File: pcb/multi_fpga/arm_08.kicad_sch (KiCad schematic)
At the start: 16 parts, among them U65 IM72D128V01XTMA1, U66 IM72D128V01XTMA1, U67 IM72D128V01XTMA1, U68 IM72D128V01XTMA1, U69 IM72D128V01XTMA1, U70 IM72D128V01XTMA1, U71 IM72D128V01XTMA1, U72 IM72D128V01XTMA1

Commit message: Fixed library and power issues.
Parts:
- C65, C66, C67, C68, C69, C70, C71, C72: symbol C -> multi_fpga:C
- U65, U66, U67, U68, U69, U70, U71, U72: symbol IM72D128 -> multi_fpga:IM72D128

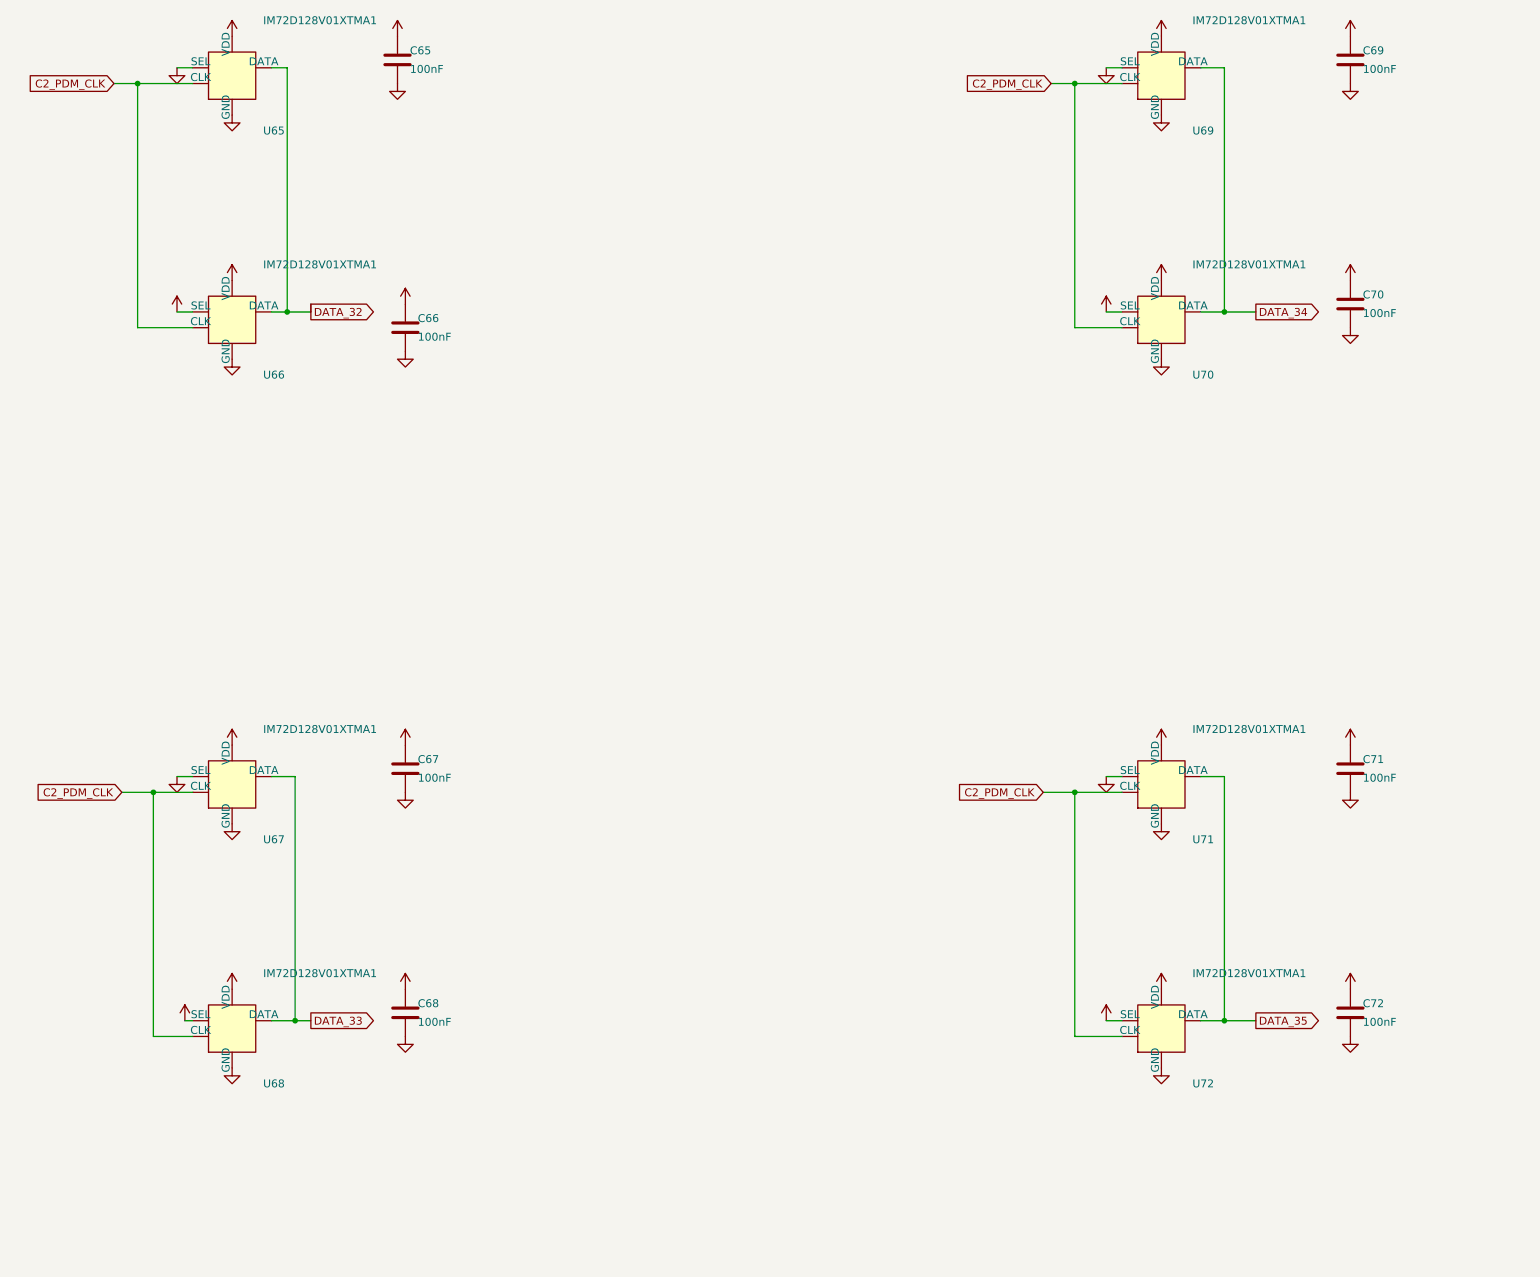
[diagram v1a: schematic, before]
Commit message: Fixed power and C ref des collisions.
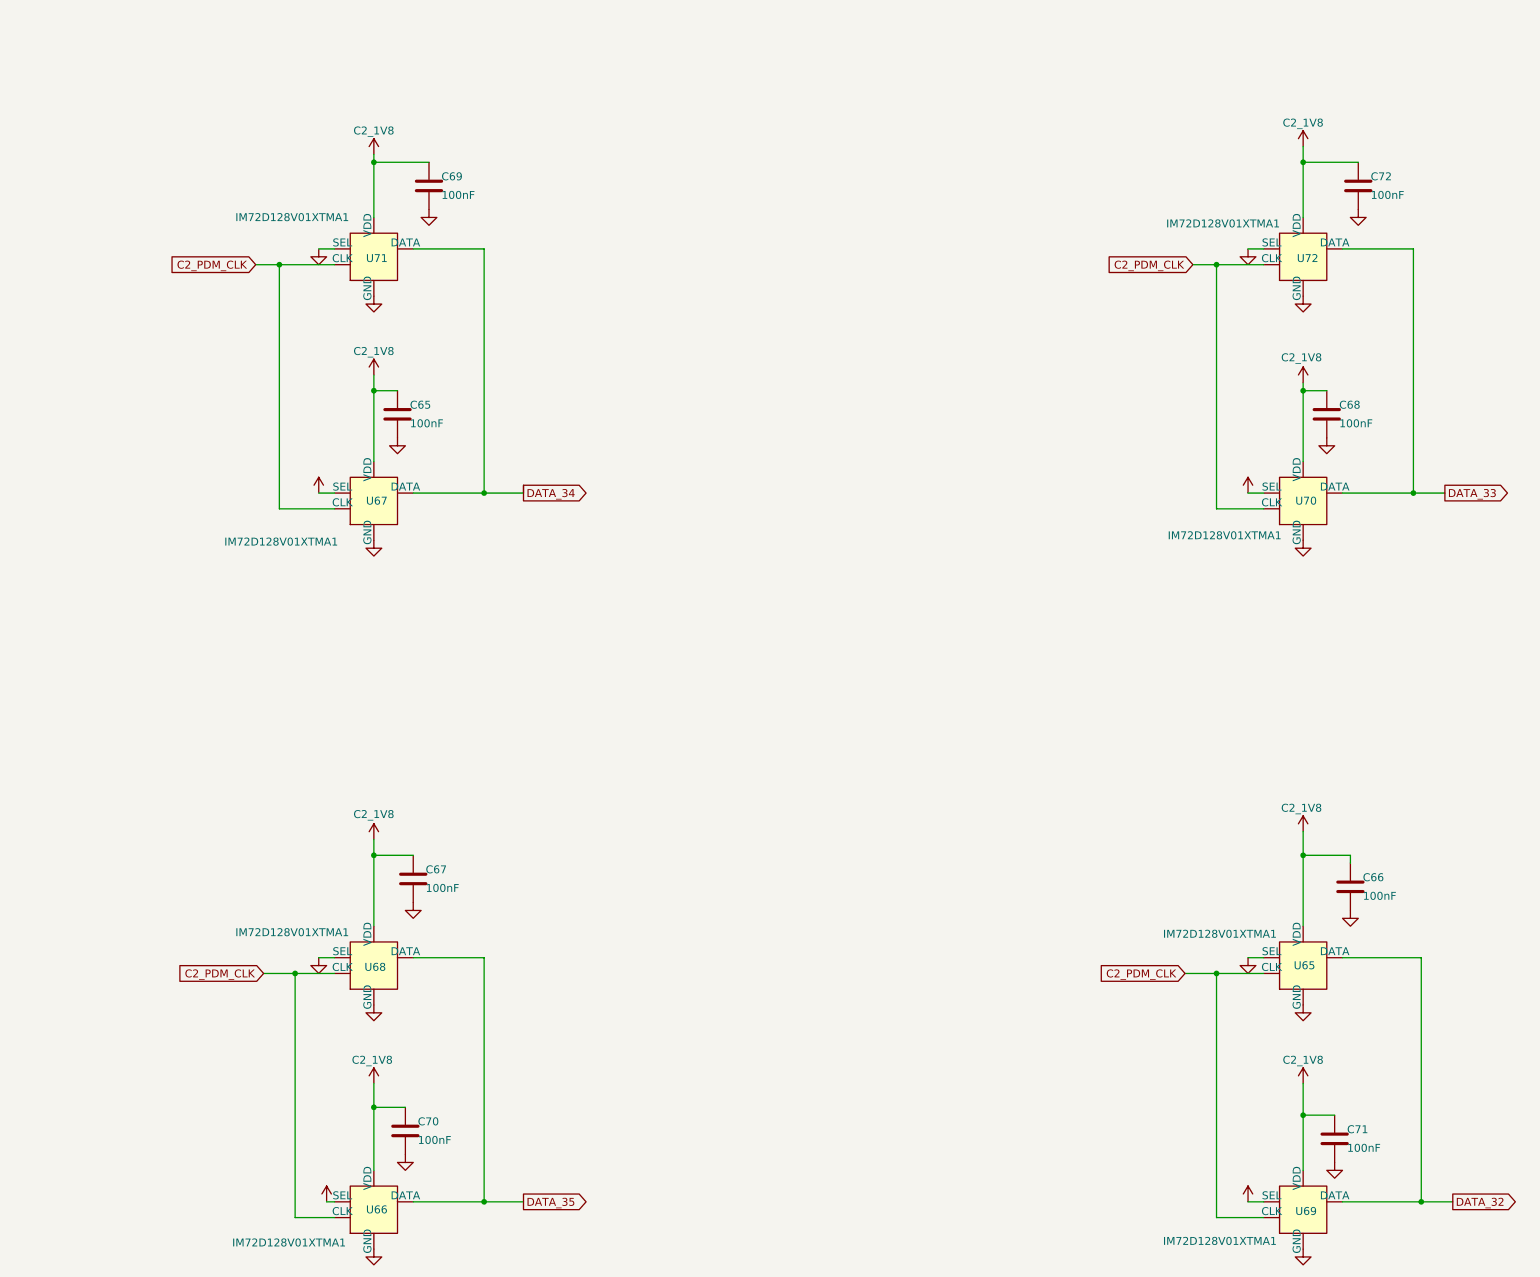
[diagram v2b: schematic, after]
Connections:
- net C2_1V8: now also U67.4 (SEL), U69.4 (SEL); no longer U68.4 (SEL), U72.4 (SEL)
- net DATA_32: now also U69.1 (DATA); no longer U66.1 (DATA)
- net DATA_33: now also U70.1 (DATA), U72.1 (DATA); no longer U67.1 (DATA), U68.1 (DATA)
- net DATA_34: now also U67.1 (DATA), U71.1 (DATA); no longer U69.1 (DATA), U70.1 (DATA)
- net DATA_35: now also U66.1 (DATA), U68.1 (DATA); no longer U71.1 (DATA), U72.1 (DATA)
- net GND: now also U68.4 (SEL), U72.4 (SEL); no longer U67.4 (SEL), U69.4 (SEL)

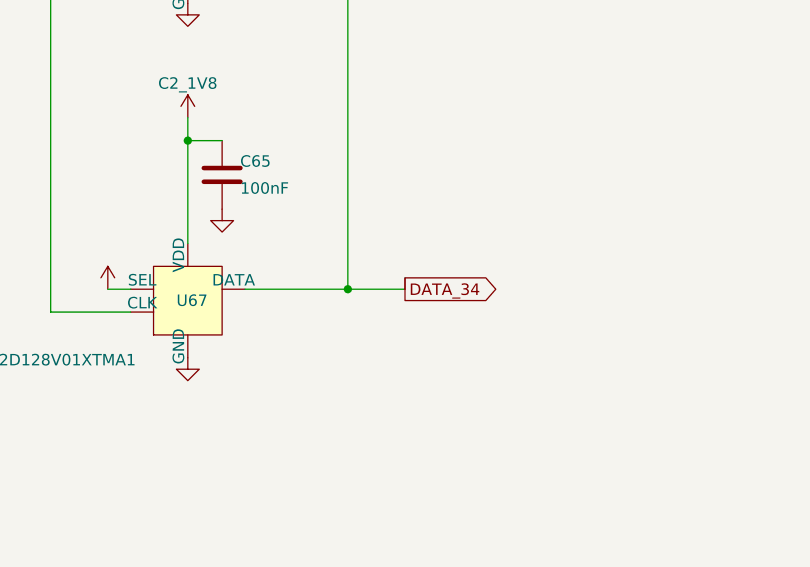
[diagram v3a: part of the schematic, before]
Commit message: Fixed regulator connection errors and dangling wire.
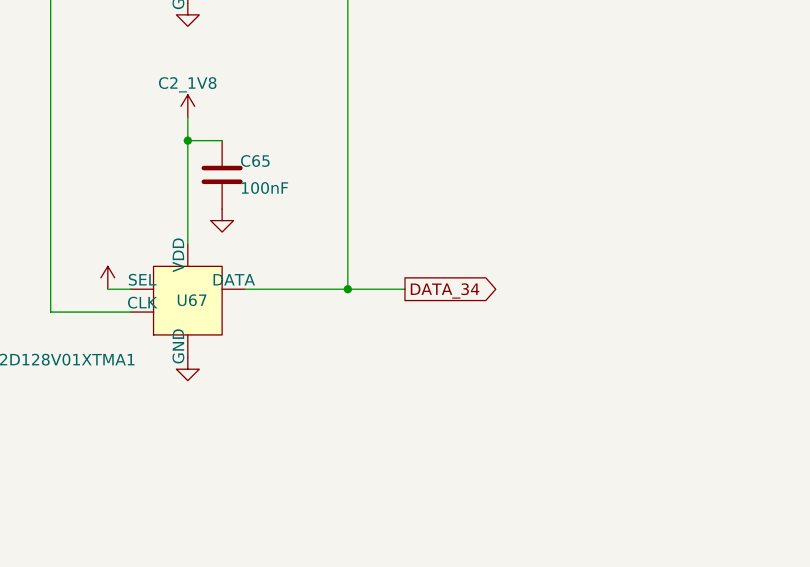
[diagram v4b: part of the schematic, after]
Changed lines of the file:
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@@
-	(wire
-		(pts
-			(xy 127 106.68) (xy 127 107.95)
-		)
-		(stroke
-			(width 0)
-			(type default)
-		)
-	)
 	(wire
 		(pts

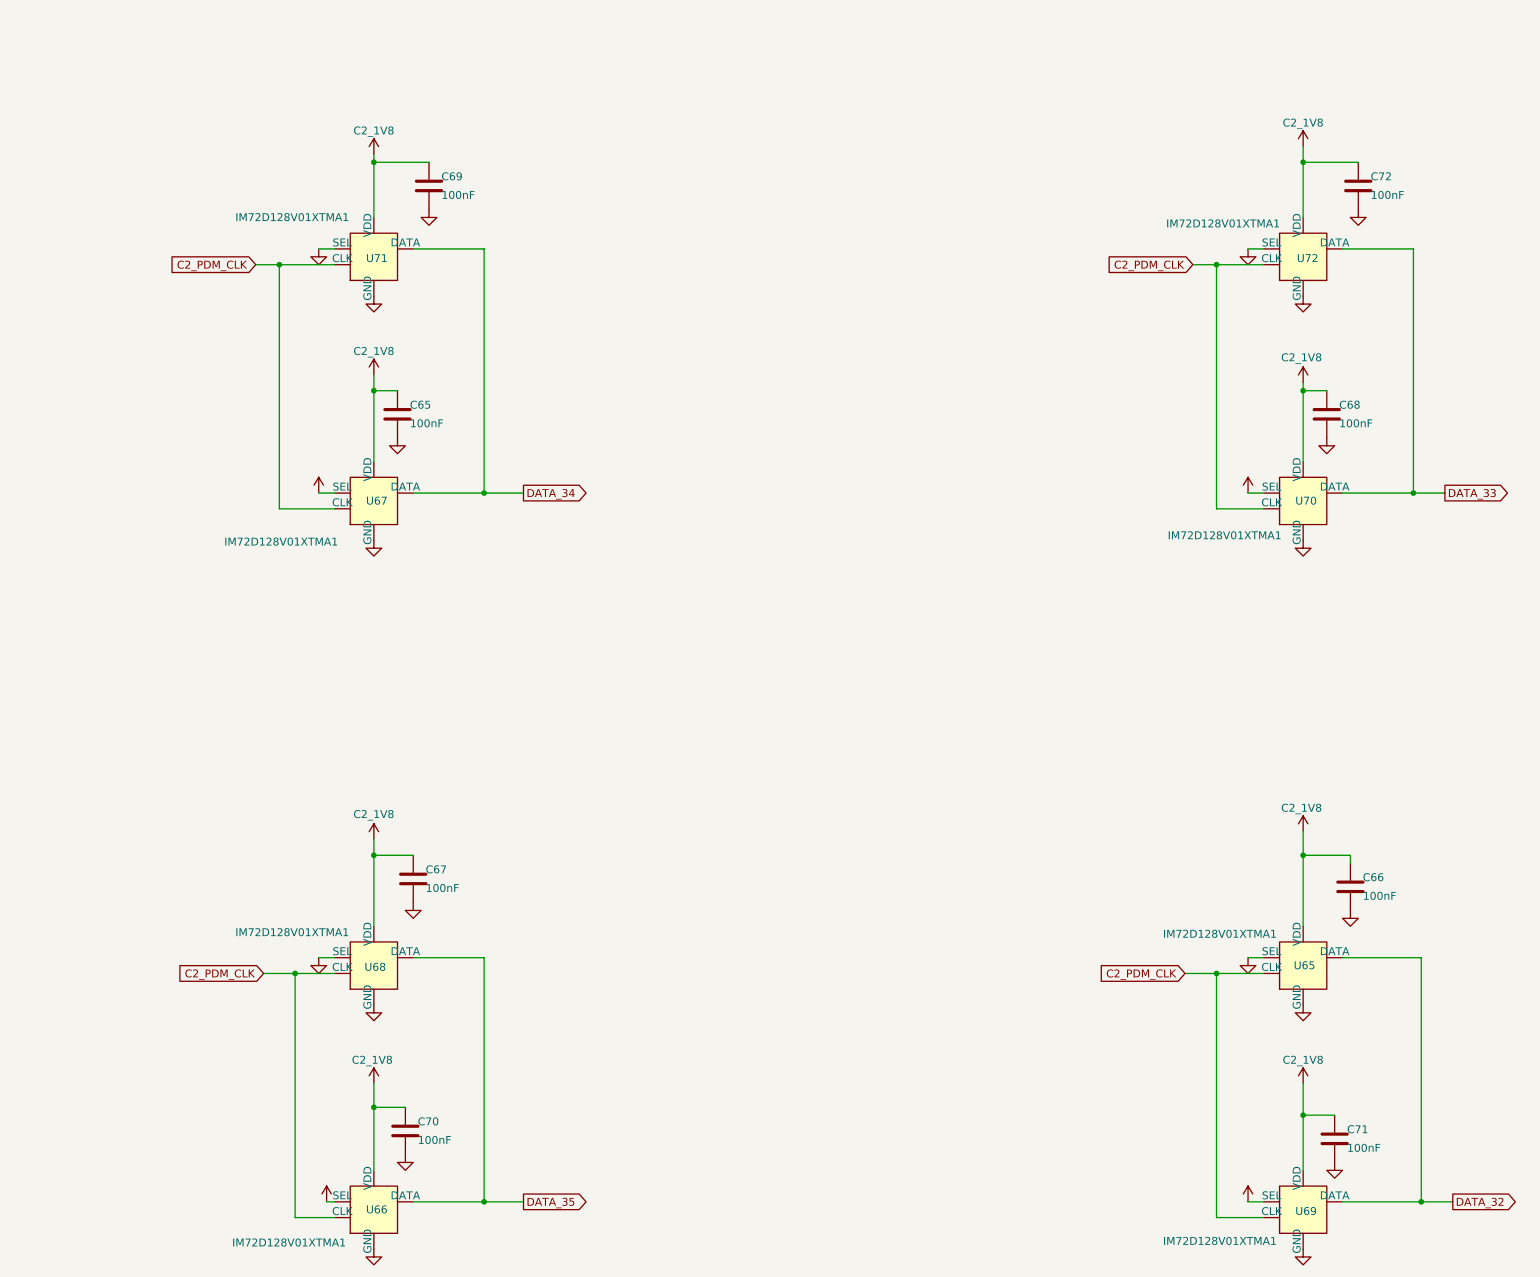
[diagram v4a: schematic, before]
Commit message: Global fix of res defs.
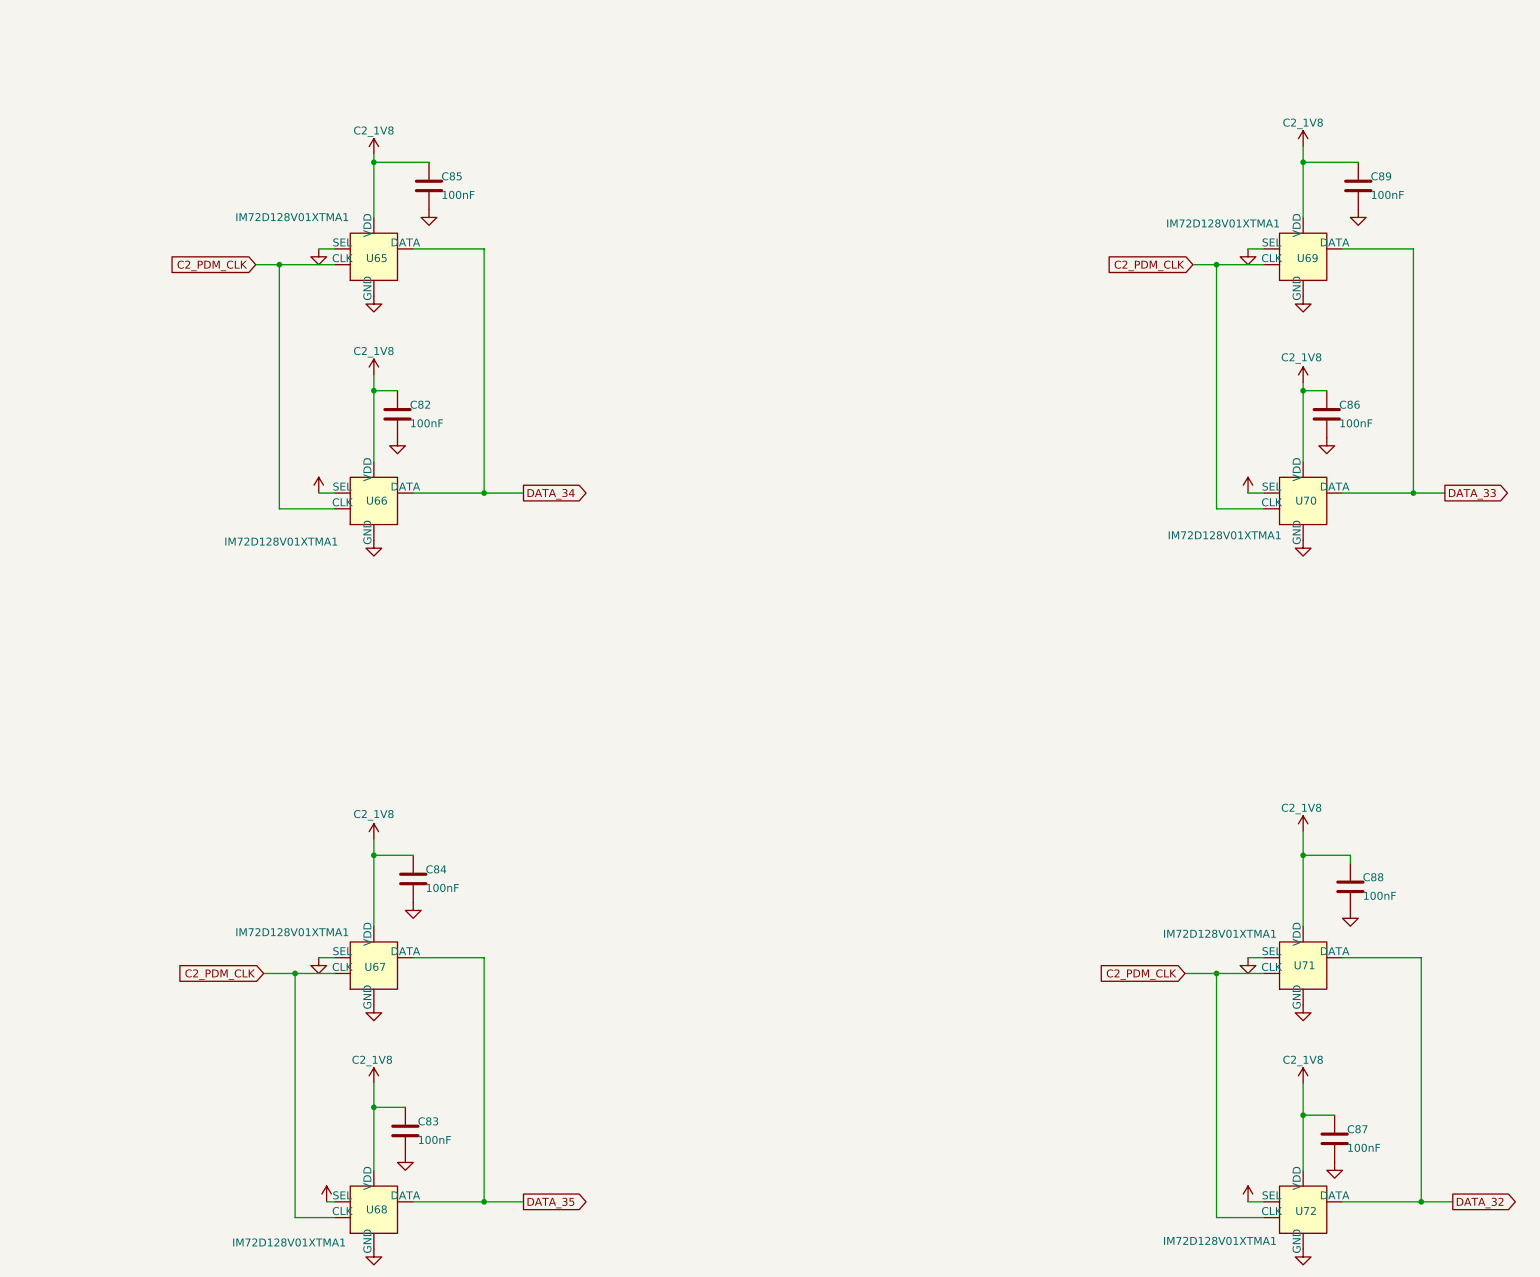
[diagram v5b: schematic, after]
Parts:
- renumbered C65 to C82, C70 to C83, C67 to C84, C69 to C85, C68 to C86, C71 to C87, C66 to C88, C72 to C89, U71 to U65, U67 to U66, U68 to U67, U66 to U68, U72 to U69, U65 to U71, U69 to U72

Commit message: Changed to use generic cap symbols and footprints.
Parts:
- C82, C83, C84, C85, C86, C87, C88, C89: symbol multi_fpga:C -> Device:C
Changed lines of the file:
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@@
 	)
 	(symbol
-		(lib_id "multi_fpga:C")
+		(lib_id "Device:C")
 		(at 106.68 95.25 0)
 		(unit 1)
@@
 		)
 		(property "Footprint" ""
-			(at 106.68 95.25 0)
+			(at 107.6452 99.06 0)
 			(hide yes)
 			(show_name no)
@@
 			)
 		)
-		(property "Description" ""
+		(property "Description" "Unpolarized capacitor"
 			(at 106.68 95.25 0)
 			(hide yes)
@@
 	)
 	(symbol
-		(lib_id "multi_fpga:C")
+		(lib_id "Device:C")
 		(at 260.35 171.45 0)
 		(unit 1)
@@
 		)
 		(property "Footprint" ""
-			(at 260.35 171.45 0)
+			(at 261.3152 175.26 0)
 			(hide yes)
 			(show_name no)
@@
 			)
 		)
-		(property "Description" ""
+		(property "Description" "Unpolarized capacitor"
 			(at 260.35 171.45 0)
 			(hide yes)
@@
 	)
 	(symbol
-		(lib_id "multi_fpga:C")
+		(lib_id "Device:C")
 		(at 261.62 58.42 0)
 		(unit 1)
@@
 		)
 		(property "Footprint" ""
-			(at 261.62 58.42 0)
+			(at 262.5852 62.23 0)
 			(hide yes)
 			(show_name no)
@@
 			)
 		)
-		(property "Description" ""
+		(property "Description" "Unpolarized capacitor"
 			(at 261.62 58.42 0)
 			(hide yes)
@@
 	)
 	(symbol
-		(lib_id "multi_fpga:C")
+		(lib_id "Device:C")
 		(at 109.22 170.18 0)
 		(unit 1)
@@
 		)
 		(property "Footprint" ""
-			(at 109.22 170.18 0)
+			(at 110.1852 173.99 0)
 			(hide yes)
 			(show_name no)
@@
 			)
 		)
-		(property "Description" ""
+		(property "Description" "Unpolarized capacitor"
 			(at 109.22 170.18 0)
 			(hide yes)
@@
 	)
 	(symbol
-		(lib_id "multi_fpga:C")
+		(lib_id "Device:C")
 		(at 256.54 95.25 0)
 		(unit 1)
@@
 		)
 		(property "Footprint" ""
-			(at 256.54 95.25 0)
+			(at 257.5052 99.06 0)
 			(hide yes)
 			(show_name no)
@@
 			)
 		)
-		(property "Description" ""
+		(property "Description" "Unpolarized capacitor"
 			(at 256.54 95.25 0)
 			(hide yes)
@@
 	)
 	(symbol
-		(lib_id "multi_fpga:C")
+		(lib_id "Device:C")
 		(at 107.95 210.82 0)
 		(unit 1)
@@
 		)
 		(property "Footprint" ""
-			(at 107.95 210.82 0)
+			(at 108.9152 214.63 0)
 			(hide yes)
 			(show_name no)
@@
 			)
 		)
-		(property "Description" ""
+		(property "Description" "Unpolarized capacitor"
 			(at 107.95 210.82 0)
 			(hide yes)
@@
 	)
 	(symbol
-		(lib_id "multi_fpga:C")
+		(lib_id "Device:C")
 		(at 257.81 212.09 0)
 		(unit 1)
@@
 		)
 		(property "Footprint" ""
-			(at 257.81 212.09 0)
+			(at 258.7752 215.9 0)
 			(hide yes)
 			(show_name no)
@@
 			)
 		)
-		(property "Description" ""
+		(property "Description" "Unpolarized capacitor"
 			(at 257.81 212.09 0)
 			(hide yes)
@@
 	)
 	(symbol
-		(lib_id "multi_fpga:C")
+		(lib_id "Device:C")
 		(at 111.76 58.42 0)
 		(unit 1)
@@
 		)
 		(property "Footprint" ""
-			(at 111.76 58.42 0)
+			(at 112.7252 62.23 0)
 			(hide yes)
 			(show_name no)
@@
 			)
 		)
-		(property "Description" ""
+		(property "Description" "Unpolarized capacitor"
 			(at 111.76 58.42 0)
 			(hide yes)
